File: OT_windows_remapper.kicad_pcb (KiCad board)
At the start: 2 copper layers, 55 x 70 mm, 68 parts, among them J1 Vcc_in, J10 Down_IN, J11 Up_IN, J12 Up_REM, J13 Down_REM, J14 CClose_IN, J15 GND, J16 12Vdc, J2 GND, J3 EPSW_aux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

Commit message: First routing
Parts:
- removed C7: 100n, Capacitor_THT:C_Rect_L7.0mm_W2.5mm_P5.00mm
- added J17: GND, Connector_Wire:SolderWire-0.75sqmm_1x01_D1.25mm_OD2.3mm, F.Cu at (145.5, 94.5)
- added J18: GND, Connector_Wire:SolderWire-2sqmm_1x01_D2mm_OD3.9mm, F.Cu at (145.5, 83.0)
- added J19: GND, Connector_Wire:SolderWire-2sqmm_1x01_D2mm_OD3.9mm, F.Cu at (145.5, 88.5)
- added J4: 12Vdc, Connector_Wire:SolderWire-2sqmm_1x01_D2mm_OD3.9mm, F.Cu at (152.0, 90.0)
- J15: value GND -> 12Vdc; footprint Connector_Wire:SolderWire-2sqmm_1x02_P7.8mm_D2mm_OD3.9mm -> Connector_Wire:SolderWire-2sqmm_1x01_D2mm_OD3.9mm
- J16: value 12Vdc -> GND; footprint Connector_Wire:SolderWire-2sqmm_1x03_P7.8mm_D2mm_OD3.9mm -> Connector_Wire:SolderWire-0.75sqmm_1x01_D1.25mm_OD2.3mm
- J2: value GND -> 12Vdc; footprint Connector_Wire:SolderWire-0.75sqmm_1x02_P4.8mm_D1.25mm_OD2.3mm -> Connector_Wire:SolderWire-2sqmm_1x01_D2mm_OD3.9mm
- U2: footprint Package_TO_SOT_THT:TO-220-3_Horizontal_TabDown -> Package_TO_SOT_THT:TO-220-3_Vertical
- moved J1 143.6 mm to (146.5, 28.0)
- moved C5 122.1 mm to (129.0, 45.0), turned to 180 degrees
- moved C1 120.5 mm to (130.5, 51.8), turned to 90 degrees
- moved C2 119.8 mm to (130.5, 54.2), turned to -90 degrees
- moved Y1 119.6 mm to (126.0, 55.0), turned to 90 degrees
- moved C3 115.2 mm to (148.5, 35.0)
- moved C6 108.2 mm to (147.5, 41.0)
- moved Q10 108.2 mm to (151.2, 72.2), turned to 90 degrees
- moved C4 103.8 mm to (147.0, 51.5), turned to 90 degrees
- moved R26 101.7 mm to (144.5, 72.5), turned to 0 degrees
- moved R25 101.6 mm to (144.5, 69.5), turned to 0 degrees
- moved J13 96.6 mm to (140.2, 94.2), turned to 90 degrees
- moved J3 96.6 mm to (151.0, 64.5), turned to 90 degrees
- moved D4 92.3 mm to (140.2, 90.7), turned to 90 degrees
- moved R6 89.6 mm to (136.5, 90.5), turned to 90 degrees
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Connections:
- C6 pad 1: Net-(C4-Pad1) -> Net-(C3-Pad1)
- J15 pad 1: GND -> Net-(J15-Pad1)
- J16 pad 1: Net-(J16-Pad1) -> GND
- J2 pad 1: GND -> Net-(J15-Pad1)
- J5 pad 1: Net-(J5-Pad1) -> GND
- J5 pad 5: GND -> Net-(J5-Pad5)
- Q4 pad 1: Net-(Q4-Pad1) -> Net-(U1-Pad6)
- Q6 pad 1: Net-(Q6-Pad1) -> Net-(U1-Pad15)
- R19 pad 1: Net-(Q4-Pad1) -> Net-(U1-Pad6)
- R21 pad 1: Net-(Q6-Pad1) -> Net-(U1-Pad15)
- R25 pad 1: Net-(J5-Pad2) -> Net-(R25-Pad1)
- U1 pad 1: Net-(J5-Pad1) -> Net-(J5-Pad5)
- U1 pad 13: Net-(Q7-Pad1) -> unconnected-(U1-Pad13)
- U1 pad 14: Net-(R13-Pad1) -> Net-(Q5-Pad1)
- U1 pad 15: Net-(R12-Pad1) -> Net-(U1-Pad15)
- U1 pad 16: Net-(R11-Pad1) -> Net-(R25-Pad1)
- U1 pad 2: unconnected-(U1-Pad2) -> Net-(R11-Pad1)
- U1 pad 21: Net-(C7-Pad1) -> unconnected-(U1-Pad21)
- U1 pad 23: Net-(Q6-Pad1) -> unconnected-(U1-Pad23)
- U1 pad 24: Net-(Q5-Pad1) -> unconnected-(U1-Pad24)
- U1 pad 25: Net-(Q4-Pad1) -> unconnected-(U1-Pad25)
- U1 pad 3: unconnected-(U1-Pad3) -> Net-(R12-Pad1)
- U1 pad 4: unconnected-(U1-Pad4) -> Net-(R13-Pad1)
- U1 pad 5: unconnected-(U1-Pad5) -> Net-(Q7-Pad1)
- U1 pad 6: unconnected-(U1-Pad6) -> Net-(U1-Pad6)
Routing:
- net Net-(C4-Pad1): track 29.6 -> 149.7 mm, vias 0 -> 1
- net Net-(U1-Pad6): track 0.00 -> 51.9 mm
- net Net-(Q8-Pad1): track 5.03 -> 45.5 mm
- net Net-(Q7-Pad1): track 5.03 -> 43.9 mm
- net Net-(J5-Pad5): track 0.00 -> 37.7 mm, vias 0 -> 1
- net Net-(Q9-Pad1): track 5.03 -> 38.3 mm
- net Net-(R13-Pad1): track 2.29 -> 27.6 mm
- net Net-(C3-Pad1): track 0.00 -> 20.6 mm
- net Net-(U1-Pad15): track 0.00 -> 17.7 mm
- net Net-(R12-Pad1): track 2.29 -> 19.7 mm
- net Net-(R11-Pad1): track 2.29 -> 19.1 mm
- net Net-(Q5-Pad1): track 5.03 -> 19.3 mm
- net Net-(J3-Pad1): track 0.00 -> 12.8 mm
- net Net-(J15-Pad1): track 0.00 -> 12.0 mm
- net Net-(C1-Pad1): track 0.00 -> 9.04 mm
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- added copper zone on B.Cu, net GND
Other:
- board size 55 x 70 mm -> 55 x 75 mm

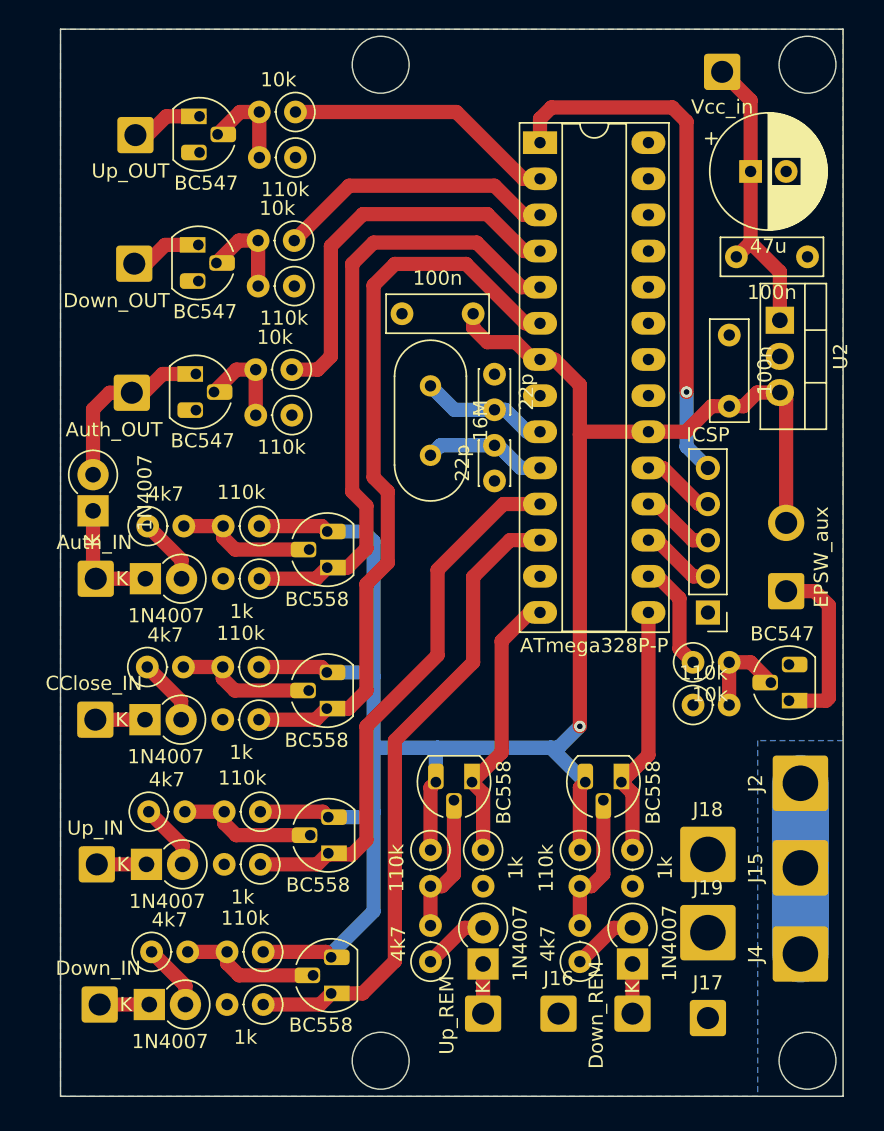
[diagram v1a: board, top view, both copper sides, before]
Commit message: Silkscreen tidied. Ready to plot.
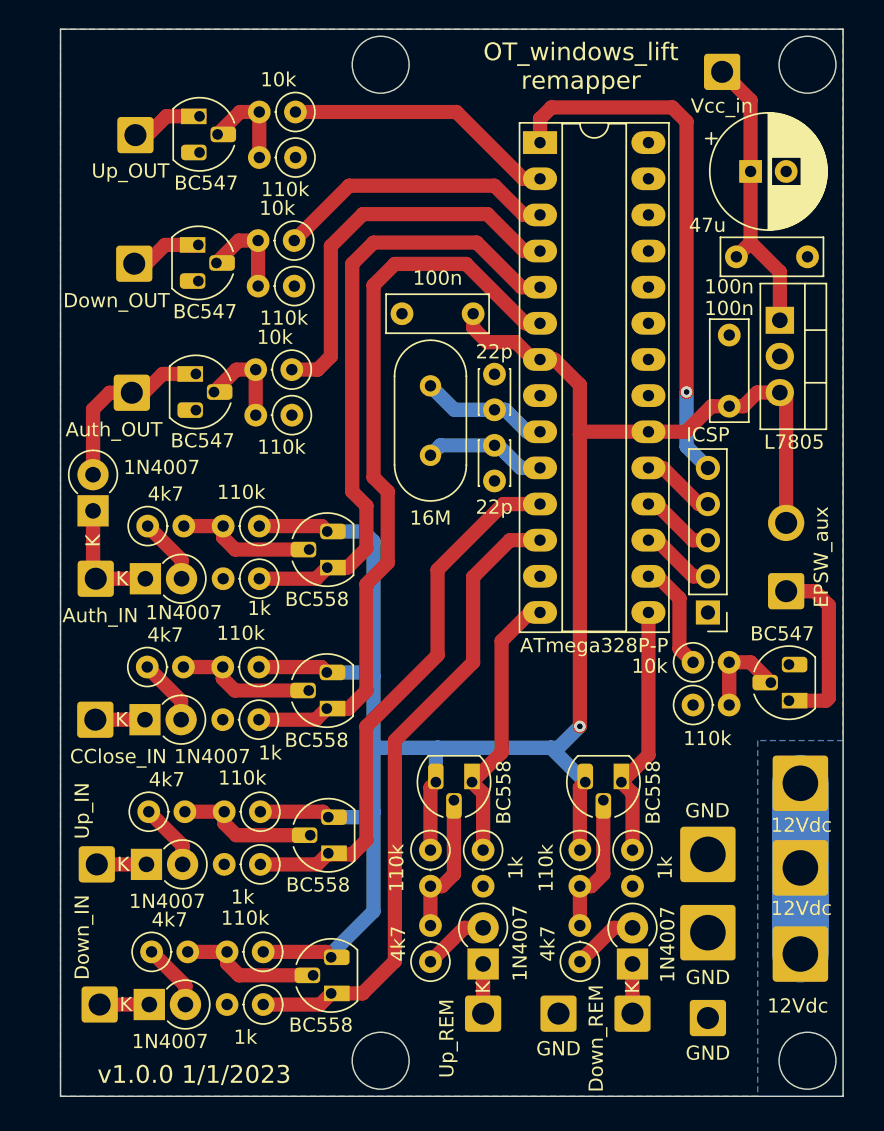
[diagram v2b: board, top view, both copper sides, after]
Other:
- board text added: "OT_windows_lift remapper"
- board text added: "v1.0.0 1/1/2023"

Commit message: plotted v1.0.0 gerbers
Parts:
- moved J1 3.16 mm to (145.5, 31.0)
- moved C3 2.06 mm to (148.0, 37.0)
- moved C1 2.00 mm to (130.5, 53.8)
- moved C2 2.00 mm to (130.5, 56.2)
- moved C4 2.00 mm to (147.0, 53.5)
- moved C5 2.00 mm to (129.0, 47.0)
- moved C6 2.00 mm to (147.5, 43.0)
- moved D1 2.00 mm to (102.3, 60.9)
- moved D2 2.00 mm to (105.9, 75.5)
- moved D3 2.00 mm to (129.7, 92.7)
- moved D4 2.00 mm to (140.2, 92.7)
- moved D6 2.00 mm to (106.2, 95.5)
- moved D7 2.00 mm to (106.0, 85.7)
- moved J10 2.00 mm to (102.8, 95.5)
- moved J11 2.00 mm to (102.5, 85.7)
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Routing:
- net Net-(C3-Pad1): track 20.6 -> 18.1 mm
- net Net-(C4-Pad1): track 149.7 -> 151.2 mm, vias 1 -> 2
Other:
- board size 55 x 75 mm -> 55 x 71 mm
- board text added: "OT_windows_lift remapper v1.0.0 3/3/2023"
- board text removed: "OT_windows_lift remapper"
- board text removed: "v1.0.0 1/1/2023"

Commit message: Included 12 V pullups resistors on board
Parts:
- removed J16: GND, Connector_Wire:SolderWire-0.75sqmm_1x01_D1.25mm_OD2.3mm
- added D10: 1N4007, Diode_THT:D_DO-41_SOD81_P2.54mm_Vertical_KathodeUp, F.Cu at (106.1, 58.0)
- added D11: 1N4007, Diode_THT:D_DO-41_SOD81_P2.54mm_Vertical_KathodeUp, F.Cu at (102.8, 92.2)
- added D12: 1N4007, Diode_THT:D_DO-41_SOD81_P2.54mm_Vertical_KathodeUp, F.Cu at (102.6, 82.3)
- added D13: 1N4007, Diode_THT:D_DO-41_SOD81_P2.54mm_Vertical_KathodeUp, F.Cu at (133.2, 92.7)
- added D8: 1N4007, Diode_THT:D_DO-41_SOD81_P2.54mm_Vertical_KathodeUp, F.Cu at (136.5, 96.2)
- added D9: 1N4007, Diode_THT:D_DO-41_SOD81_P2.54mm_Vertical_KathodeUp, F.Cu at (102.6, 72.1)
- added R27: 2k7, Resistor_THT:R_Axial_DIN0207_L6.3mm_D2.5mm_P2.54mm_Vertical, F.Cu at (126.4, 98.0)
- added R28: 2k7, Resistor_THT:R_Axial_DIN0207_L6.3mm_D2.5mm_P2.54mm_Vertical, F.Cu at (106.2, 68.8)
- added R29: 2k7, Resistor_THT:R_Axial_DIN0207_L6.3mm_D2.5mm_P2.54mm_Vertical, F.Cu at (112.2, 58.0)
- added R30: 2k7, Resistor_THT:R_Axial_DIN0207_L6.3mm_D2.5mm_P2.54mm_Vertical, F.Cu at (106.4, 88.8)
- added R31: 2k7, Resistor_THT:R_Axial_DIN0207_L6.3mm_D2.5mm_P2.54mm_Vertical, F.Cu at (106.2, 78.8)
- added R32: 2k7, Resistor_THT:R_Axial_DIN0207_L6.3mm_D2.5mm_P2.54mm_Vertical, F.Cu at (133.2, 86.8)
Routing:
- net Net-(C3-Pad1): track 18.1 -> 186.4 mm, vias 0 -> 8
- net Net-(C4-Pad1): track 151.2 -> 171.9 mm, vias 2 -> 1
- net Net-(D8-Pad2): track 0.00 -> 9.95 mm
- net Net-(D1-Pad1): track 8.34 -> 13.5 mm
- net Net-(D11-Pad2): track 0.00 -> 3.96 mm
- net Net-(D12-Pad2): track 0.00 -> 3.94 mm
- net Net-(D9-Pad2): track 0.00 -> 3.86 mm
- net Net-(D4-Pad1): track 3.49 -> 7.23 mm
- net Net-(D2-Pad1): track 3.49 -> 7.02 mm
- net Net-(D3-Pad1): track 3.49 -> 7.00 mm
- net Net-(D10-Pad2): track 0.00 -> 3.48 mm
- net Net-(D7-Pad1): track 3.49 -> 6.94 mm
- net Net-(D6-Pad1): track 3.49 -> 6.86 mm
- net Net-(D13-Pad2): track 0.00 -> 3.28 mm
- net Net-(Q8-Pad1): track 45.5 -> 44.6 mm
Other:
- board text added: "OT_windows_lift remapper v1.1.0 23/7/2023"
- board text removed: "OT_windows_lift remapper v1.0.0 3/3/2023"
